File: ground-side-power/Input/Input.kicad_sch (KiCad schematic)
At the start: 36 parts, among them J1 Battery Terminals, J2 Battery Terminals, J26 Conn_01x02_Female, J3 Battery Terminals, J4 Battery Terminals, J5 874270842, J6 874270842, J7 ATX-24, J8 Conn_01x03_Female, J9 Conn_01x03_Female, K1 AZ2150-1A-12DEF, M1 Fan_PC_Chassis, SW1 GRB234A2NABA1, U1 INA180, U2 INA180

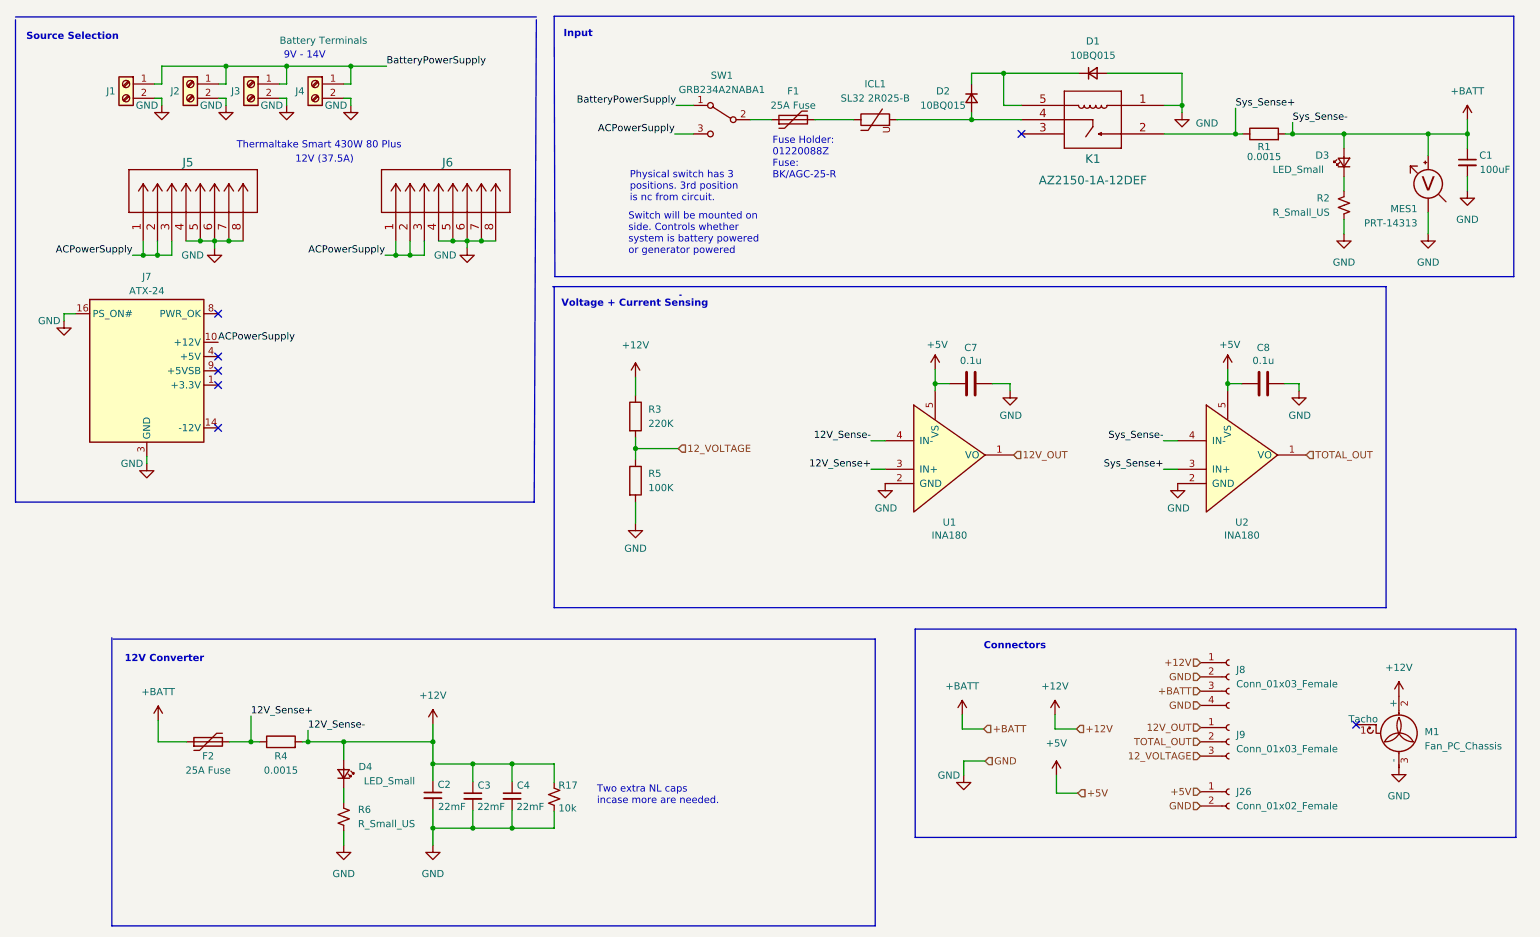
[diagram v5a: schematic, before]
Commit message: Updated Fuses
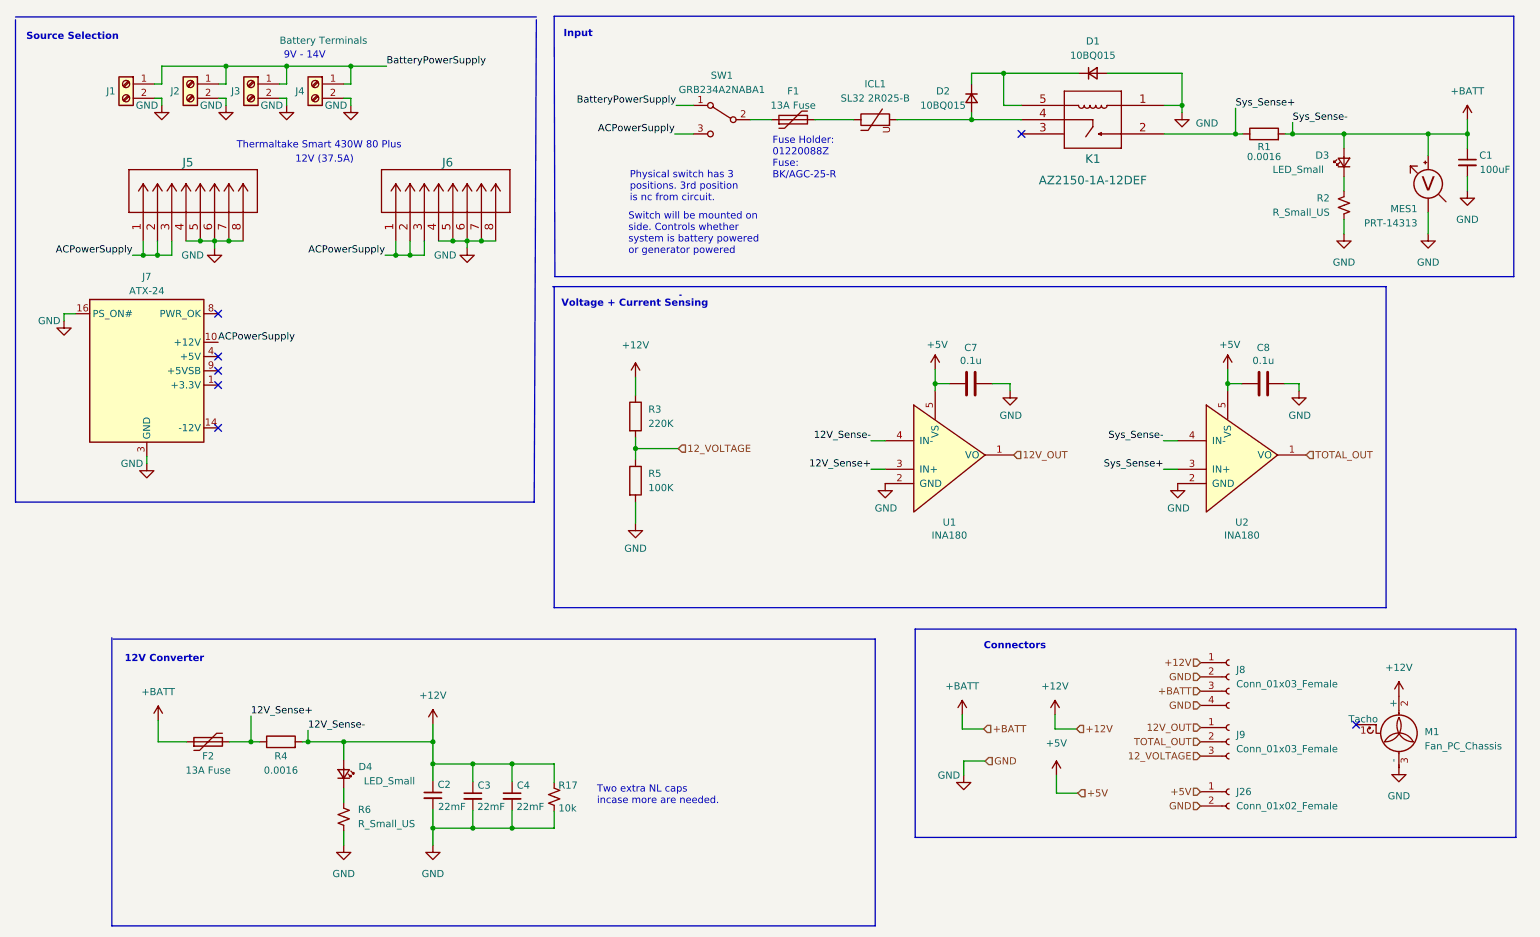
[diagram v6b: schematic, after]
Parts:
- F1, F2: value 25A Fuse -> 13A Fuse
- J8: footprint GSP:CUI_TB008A-508-04BE -> GSP:1935323
- R1, R4: value 0.0015 -> 0.0016; footprint Resistor_SMD:R_2512_6332Metric_Pad1.40x3.35mm_HandSolder -> Resistor_SMD:R_1206_3216Metric_Pad1.30x1.75mm_HandSolder
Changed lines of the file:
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@@
     (in_bom yes) (on_board yes)
     (property "Reference" "R1" (id 0) (at 237.363 40.259 90))
-    (property "Value" "0.0015" (id 1) (at 237.363 42.037 90))
-    (property "Footprint" "Resistor_SMD:R_2512_6332Metric_Pad1.40x3.35mm_HandSolder" (id 2) (at 237.363 39.751 90)
+    (property "Value" "0.0016" (id 1) (at 237.363 42.037 90))
+    (property "Footprint" "Resistor_SMD:R_1206_3216Metric_Pad1.30x1.75mm_HandSolder" (id 2) (at 237.363 39.751 90)
       (effects (font (size 1.27 1.27)) hide)
     )
@@
     (in_bom yes) (on_board yes)
     (property "Reference" "F2" (id 0) (at 49.403 148.717 90))
-    (property "Value" "25A Fuse" (id 1) (at 49.403 151.257 90))
+    (property "Value" "13A Fuse" (id 1) (at 49.403 151.257 90))
     (property "Footprint" "Fuse:Fuseholder_Clip-6.3x32mm_Littelfuse_102_122_Inline_P34.21x7.62mm_D1.98mm_Horizontal" (id 2) (at 54.483 144.907 0)
       (effects (font (size 1.27 1.27)) (justify left) hide)
@@
     (in_bom yes) (on_board yes)
     (property "Reference" "R4" (id 0) (at 62.357 148.717 90))
-    (property "Value" "0.0015" (id 1) (at 62.357 151.257 90))
-    (property "Footprint" "Resistor_SMD:R_2512_6332Metric_Pad1.40x3.35mm_HandSolder" (id 2) (at 62.357 147.955 90)
+    (property "Value" "0.0016" (id 1) (at 62.357 151.257 90))
+    (property "Footprint" "Resistor_SMD:R_1206_3216Metric_Pad1.30x1.75mm_HandSolder" (id 2) (at 62.357 147.955 90)
       (effects (font (size 1.27 1.27)) hide)
     )
@@
     (in_bom yes) (on_board yes)
     (property "Reference" "F1" (id 0) (at 153.543 30.353 90))
-    (property "Value" "25A Fuse" (id 1) (at 153.543 32.893 90))
+    (property "Value" "13A Fuse" (id 1) (at 153.543 32.893 90))
     (property "Footprint" "Fuse:Fuseholder_Clip-6.3x32mm_Littelfuse_102_122_Inline_P34.21x7.62mm_D1.98mm_Horizontal" (id 2) (at 158.623 34.163 0)
       (effects (font (size 1.27 1.27)) (justify left) hide)
@@
       (effects (font (size 1.27 1.27)) (justify left))
     )
-    (property "Footprint" "GSP:CUI_TB008A-508-04BE" (id 2) (at 231.14 134.62 0)
-      (effects (font (size 1.27 1.27)) hide)
-    )
+    (property "Footprint" "GSP:1935323" (id 2) (at 231.14 134.62 0)
+      (effects (font (size 1.27 1.27)) hide)
+    )

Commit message: Updated schematic to have matching fuse values
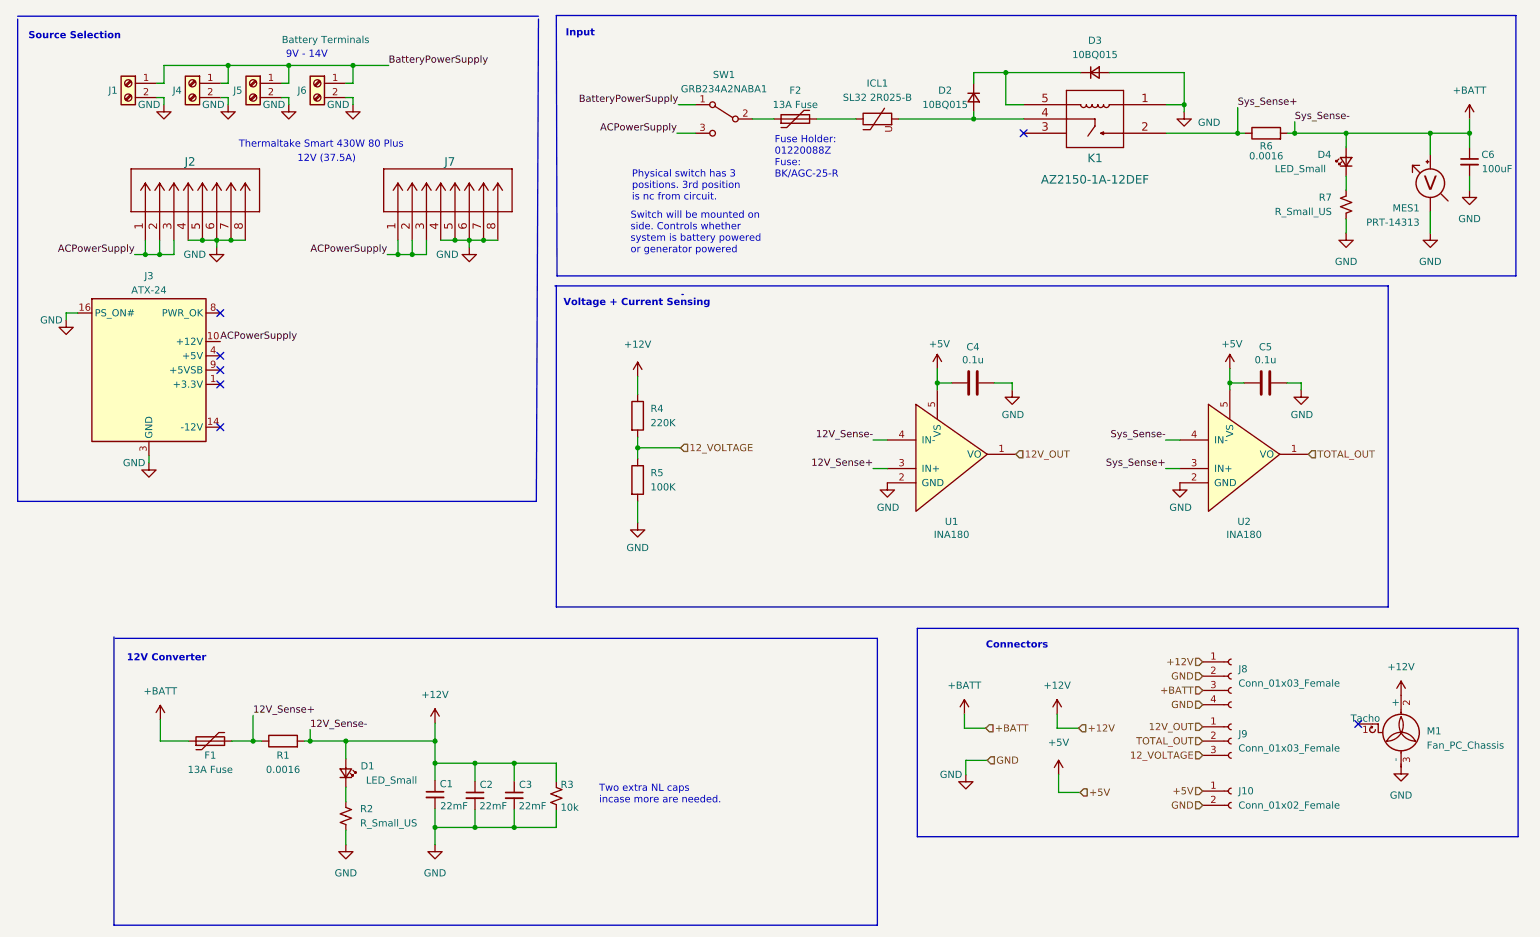
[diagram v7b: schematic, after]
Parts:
- removed C4: 22mF, GSP:LLS1C223MELZ, symbol Device:C_Small
- removed C7, C8: 0.1u, Capacitor_SMD:C_0805_2012Metric_Pad1.18x1.45mm_HandSolder, symbol Device:C
- removed D1: 10BQ015, Diode_SMD:D_SMB_Handsoldering, symbol Device:D_Small
- removed D3: LED_Small, Diode_SMD:D_1206_3216Metric_Pad1.42x1.75mm_HandSolder, symbol Device:LED_Small
- removed J2, J3: Battery Terminals, GSP:1935310, symbol Connector:Screw_Terminal_01x02
- removed J26: Conn_01x02_Female, GSP:1935310, symbol Connector:Conn_01x02_Female
- removed J5, J6: 874270842, GSP:MOLEX_874270842, symbol GSP:455860005
- removed J7: ATX-24, GSP:MOLEX_442060001, symbol Connector:ATX-24
- removed R17: 10k, Resistor_SMD:R_0805_2012Metric_Pad1.20x1.40mm_HandSolder, symbol Device:R_Small_US
- removed R3: 220K, Resistor_SMD:R_0805_2012Metric_Pad1.20x1.40mm_HandSolder, symbol Device:R
- removed R6: R_Small_US, Resistor_SMD:R_0805_2012Metric_Pad1.20x1.40mm_HandSolder, symbol Device:R_Small_US
- added C4, C5: 0.1u, Capacitor_SMD:C_0805_2012Metric_Pad1.18x1.45mm_HandSolder, symbol Device:C
- added C6: 100uF, Capacitor_THT:CP_Radial_D6.3mm_P2.50mm, symbol Device:C_Small
- added D1: LED_Small, Diode_SMD:D_1206_3216Metric_Pad1.42x1.75mm_HandSolder, symbol Device:LED_Small
- added D3: 10BQ015, Diode_SMD:D_SMB_Handsoldering, symbol Device:D_Small
- added J10: Conn_01x02_Female, GSP:1935310, symbol Connector:Conn_01x02_Female
- added J2, J7: 874270842, GSP:MOLEX_874270842, symbol GSP:455860005
- added J3: ATX-24, GSP:MOLEX_442060001, symbol Connector:ATX-24
- added J5, J6: Battery Terminals, GSP:1935310, symbol Connector:Screw_Terminal_01x02
- added R3: 10k, Resistor_SMD:R_0805_2012Metric_Pad1.20x1.40mm_HandSolder, symbol Device:R_Small_US
- added R6: 0.0016, Resistor_SMD:R_1206_3216Metric_Pad1.30x1.75mm_HandSolder, symbol Device:R
- added R7: R_Small_US, Resistor_SMD:R_0805_2012Metric_Pad1.20x1.40mm_HandSolder, symbol Device:R_Small_US
- C1: value 100uF -> 22mF; footprint Capacitor_THT:CP_Radial_D6.3mm_P2.50mm -> GSP:LLS1C223MELZ
- R4: value 0.0016 -> 220K; footprint Resistor_SMD:R_1206_3216Metric_Pad1.30x1.75mm_HandSolder -> Resistor_SMD:R_0805_2012Metric_Pad1.20x1.40mm_HandSolder
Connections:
- net +12V: now also C1.1, R1.2, R4.1, D1.2 (A), R3.1; no longer D4.2 (A), R4.2
- net +5V: now also C4.2, C5.2, J10.1 (Pin_1)
- net +BATT: now also D4.2 (A), F1.1, C6.1, R6.2; no longer C1.1, F2.1, R1.2
- net 12V_Sense+: now also F1.2, R1.1; no longer F2.2, R4.1
- net 12_VOLTAGE: now also R4.2
- net ACPowerSupply: now also J2.1, J2.2, J2.3, J3.10 (+12V), J3.11 (+12V), J7.1, J7.2, J7.3
- net BatteryPowerSupply: now also J5.1 (Pin_1), J6.1 (Pin_1)
- net GND: now also C4.1, C5.1, C6.2, D3.2 (A), J10.2 (Pin_2), J2.4, J2.5, J2.6, J2.7, J2.8, J3.15 (GND), J3.16 (PS_ON#), J3.17 (GND), J3.18 (GND), J3.19 (GND), J3.24 (GND), J3.3 (GND), J3.5 (GND), J3.7 (GND), J5.2 (Pin_2), J6.2 (Pin_2), J7.4, J7.5, J7.6, J7.7, J7.8, R3.2, R7.1
- net Sys_Sense+: now also R6.1; no longer R1.1
- net at R2.2: now also D1.1 (K)
- net at D4.1 (K): now also R7.2
- net at D2.1 (K), K1.5: now also D3.1 (K)
- net at ICL1.1: now also F2.2; no longer F1.2
- net at SW1.2 (B): now also F2.1; no longer F1.1
- new net: J3.1 (+3.3V), J3.12 (+3.3V), J3.13 (+3.3V), J3.2 (+3.3V)
- new net: J3.21 (+5V), J3.22 (+5V), J3.23 (+5V), J3.4 (+5V), J3.6 (+5V)
